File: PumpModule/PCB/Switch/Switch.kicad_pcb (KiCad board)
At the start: 2 copper layers, 47 x 4.4 mm, 3 parts, among them J1 Conn_01x03, SW1 SW_Wuerth_450301014042, SW2 SW_Wuerth_450301014042

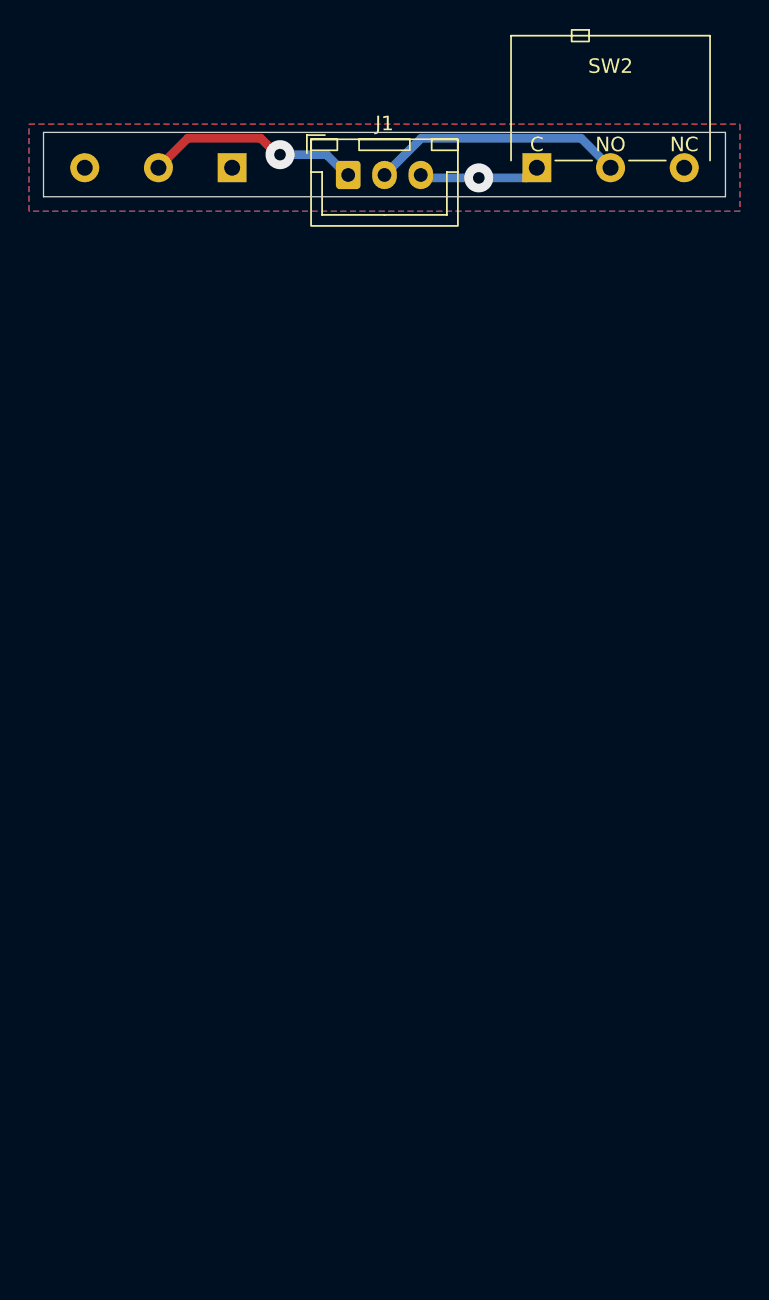
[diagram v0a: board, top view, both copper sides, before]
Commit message: [PumpModule][PCB] Add switch v1.2 manufacturing files
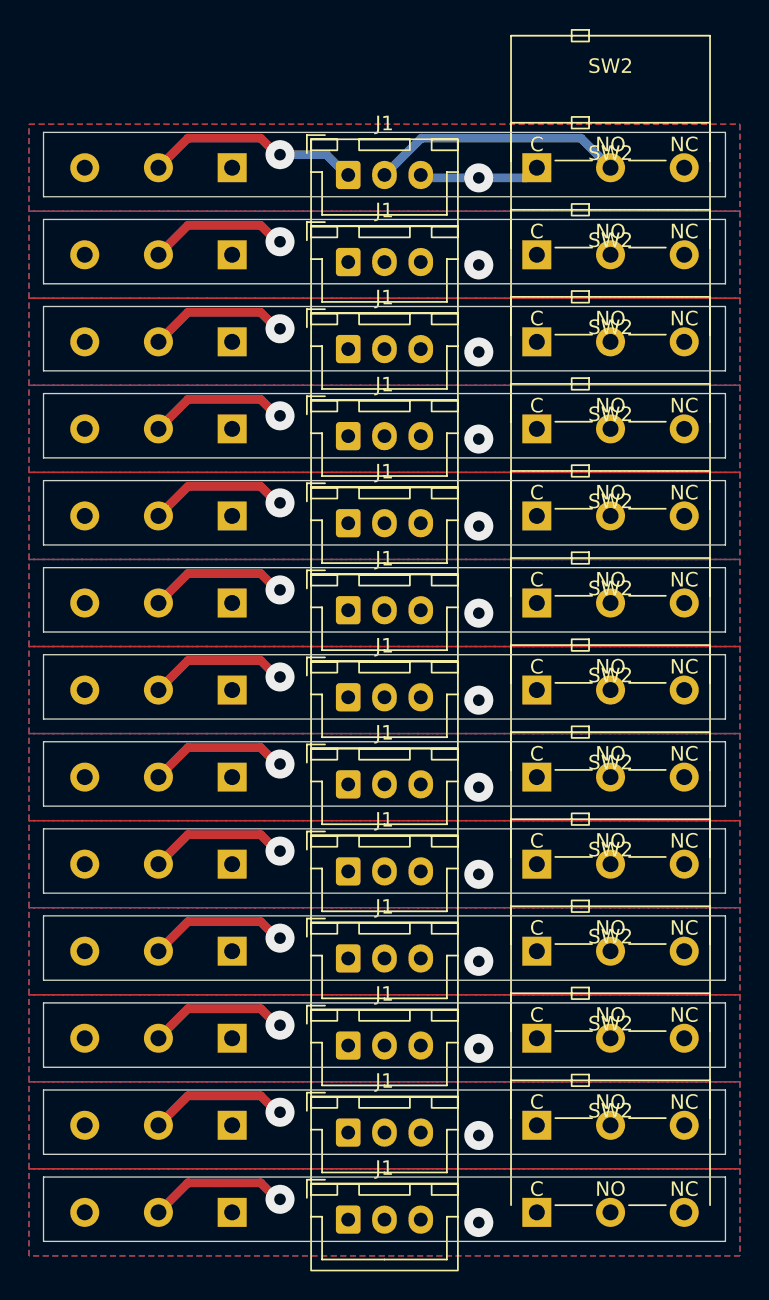
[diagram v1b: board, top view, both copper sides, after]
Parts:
- added J1: Conn_01x03, Connector_JST:JST_XH_B3B-XH-A_1x03_P2.50mm_Vertical, F.Cu at (90.0, 102.5)
- added J1: Conn_01x03, Connector_JST:JST_XH_B3B-XH-A_1x03_P2.50mm_Vertical, F.Cu at (90.0, 126.5)
- added J1: Conn_01x03, Connector_JST:JST_XH_B3B-XH-A_1x03_P2.50mm_Vertical, F.Cu at (90.0, 78.5)
- added J1: Conn_01x03, Connector_JST:JST_XH_B3B-XH-A_1x03_P2.50mm_Vertical, F.Cu at (90.0, 114.5)
- added J1: Conn_01x03, Connector_JST:JST_XH_B3B-XH-A_1x03_P2.50mm_Vertical, F.Cu at (90.0, 120.5)
- added J1: Conn_01x03, Connector_JST:JST_XH_B3B-XH-A_1x03_P2.50mm_Vertical, F.Cu at (90.0, 90.5)
- added J1: Conn_01x03, Connector_JST:JST_XH_B3B-XH-A_1x03_P2.50mm_Vertical, F.Cu at (90.0, 132.5)
- added J1: Conn_01x03, Connector_JST:JST_XH_B3B-XH-A_1x03_P2.50mm_Vertical, F.Cu at (90.0, 144.5)
- added J1: Conn_01x03, Connector_JST:JST_XH_B3B-XH-A_1x03_P2.50mm_Vertical, F.Cu at (90.0, 84.5)
- added J1: Conn_01x03, Connector_JST:JST_XH_B3B-XH-A_1x03_P2.50mm_Vertical, F.Cu at (90.0, 138.5)
- added J1: Conn_01x03, Connector_JST:JST_XH_B3B-XH-A_1x03_P2.50mm_Vertical, F.Cu at (90.0, 96.5)
- added J1: Conn_01x03, Connector_JST:JST_XH_B3B-XH-A_1x03_P2.50mm_Vertical, F.Cu at (90.0, 108.5)
- added SW1: SW_Wuerth_450301014042, Button_Switch_THT:SW_XKB_DM1-16UC-1, B.Cu at (82.0, 90.0)
- added SW1: SW_Wuerth_450301014042, Button_Switch_THT:SW_XKB_DM1-16UC-1, B.Cu at (82.0, 120.0)
- added SW1: SW_Wuerth_450301014042, Button_Switch_THT:SW_XKB_DM1-16UC-1, B.Cu at (82.0, 126.0)
- added SW1: SW_Wuerth_450301014042, Button_Switch_THT:SW_XKB_DM1-16UC-1, B.Cu at (82.0, 138.0)
- added SW1: SW_Wuerth_450301014042, Button_Switch_THT:SW_XKB_DM1-16UC-1, B.Cu at (82.0, 84.0)
- added SW1: SW_Wuerth_450301014042, Button_Switch_THT:SW_XKB_DM1-16UC-1, B.Cu at (82.0, 144.0)
- added SW1: SW_Wuerth_450301014042, Button_Switch_THT:SW_XKB_DM1-16UC-1, B.Cu at (82.0, 78.0)
- added SW1: SW_Wuerth_450301014042, Button_Switch_THT:SW_XKB_DM1-16UC-1, B.Cu at (82.0, 108.0)
- added SW1: SW_Wuerth_450301014042, Button_Switch_THT:SW_XKB_DM1-16UC-1, B.Cu at (82.0, 96.0)
- added SW1: SW_Wuerth_450301014042, Button_Switch_THT:SW_XKB_DM1-16UC-1, B.Cu at (82.0, 102.0)
- added SW1: SW_Wuerth_450301014042, Button_Switch_THT:SW_XKB_DM1-16UC-1, B.Cu at (82.0, 114.0)
- added SW1: SW_Wuerth_450301014042, Button_Switch_THT:SW_XKB_DM1-16UC-1, B.Cu at (82.0, 132.0)
- added SW2: SW_Wuerth_450301014042, Button_Switch_THT:SW_XKB_DM1-16UC-1, F.Cu at (103.0, 102.0)
- added SW2: SW_Wuerth_450301014042, Button_Switch_THT:SW_XKB_DM1-16UC-1, F.Cu at (103.0, 144.0)
- added SW2: SW_Wuerth_450301014042, Button_Switch_THT:SW_XKB_DM1-16UC-1, F.Cu at (103.0, 78.0)
- added SW2: SW_Wuerth_450301014042, Button_Switch_THT:SW_XKB_DM1-16UC-1, F.Cu at (103.0, 84.0)
- added SW2: SW_Wuerth_450301014042, Button_Switch_THT:SW_XKB_DM1-16UC-1, F.Cu at (103.0, 96.0)
- added SW2: SW_Wuerth_450301014042, Button_Switch_THT:SW_XKB_DM1-16UC-1, F.Cu at (103.0, 126.0)
- added SW2: SW_Wuerth_450301014042, Button_Switch_THT:SW_XKB_DM1-16UC-1, F.Cu at (103.0, 138.0)
- added SW2: SW_Wuerth_450301014042, Button_Switch_THT:SW_XKB_DM1-16UC-1, F.Cu at (103.0, 120.0)
- added SW2: SW_Wuerth_450301014042, Button_Switch_THT:SW_XKB_DM1-16UC-1, F.Cu at (103.0, 132.0)
- added SW2: SW_Wuerth_450301014042, Button_Switch_THT:SW_XKB_DM1-16UC-1, F.Cu at (103.0, 114.0)
- added SW2: SW_Wuerth_450301014042, Button_Switch_THT:SW_XKB_DM1-16UC-1, F.Cu at (103.0, 90.0)
- added SW2: SW_Wuerth_450301014042, Button_Switch_THT:SW_XKB_DM1-16UC-1, F.Cu at (103.0, 108.0)
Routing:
- net Net-(J1-Pin_1): track 15.0 -> 131.3 mm, vias 1 -> 13
- net GND: vias 1 -> 13
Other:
- board size 47 x 4.4 mm -> 47 x 76.4 mm

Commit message: [PumpModule][PCB] Create Switch PCB manufacturing files
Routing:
- net Net-(J1-Pin_2): track 17.5 -> 227.1 mm
- net GND: track 8.37 -> 108.8 mm
- net Net-(J1-Pin_1): track 131.3 -> 194.6 mm
